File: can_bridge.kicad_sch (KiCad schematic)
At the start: 1 part, among them J9 Conn_01x05_Pin

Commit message: use Common libraries, replace TI MCU with STM32 for CAN bridge
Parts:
- J9: footprint (none) -> Connector_PinHeader_2.54mm:PinHeader_1x05_P2.54mm_Vertical
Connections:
- no-connect marks 2 -> 0
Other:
- removed sheet USB Connector
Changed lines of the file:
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@@
 		(color 0 0 0 0)
 	)
-	(junction
-		(at 84.455 69.215)
-		(diameter 0)
-		(color 0 0 0 0)
-	)
-	(junction
-		(at 84.455 62.865)
-		(diameter 0)
-		(color 0 0 0 0)
-	)
-	(no_connect
-		(at 212.09 82.55)
-	)
-	(no_connect
-		(at 212.09 85.725)
-	)
 	(wire
 		(pts
@@
 	(wire
 		(pts
-			(xy 84.455 62.865) (xy 84.455 69.215)
-		)
-		(stroke
-			(width 0)
-			(type default)
-		)
-	)
-	(wire
-		(pts
 			(xy 84.455 62.865) (xy 116.205 62.865)
 		)
@@
 	(wire
 		(pts
-			(xy 176.53 85.725) (xy 180.975 85.725)
-		)
-		(stroke
-			(width 0)
-			(type default)
-		)
-	)
-	(wire
-		(pts
 			(xy 111.76 41.91) (xy 116.205 41.91)
 		)
@@
 		(pts
 			(xy 25.4 57.785) (xy 36.195 57.785)
-		)
-		(stroke
-			(width 0)
-			(type default)
-		)
-	)
-	(wire
-		(pts
-			(xy 176.53 82.55) (xy 180.975 82.55)
 		)
 		(stroke
@@
 			)
 			(justify right)
-		)
-	)
-	(hierarchical_label "GND"
-		(shape input)
-		(at 212.09 88.9 0)
-		(fields_autoplaced yes)
-		(effects
-			(font
-				(size 1.524 1.524)
-			)
-			(justify left)
-		)
-	)
-	(hierarchical_label "GND"
-		(shape input)
-		(at 212.09 92.075 0)
-		(fields_autoplaced yes)
-		(effects
-			(font
-				(size 1.524 1.524)
-			)
-			(justify left)
 		)
 	)
@@
 			)
 		)
-		(property "Footprint" ""
+		(property "Footprint" "Connector_PinHeader_2.54mm:PinHeader_1x05_P2.54mm_Vertical"
 			(at 200.66 62.865 0)
 			(effects
@@
 	)
 	(sheet
-		(at 180.975 78.105)
-		(size 31.115 16.51)
-		(fields_autoplaced yes)
-		(stroke
-			(width 0.1524)
-			(type solid)
-		)
-		(fill
-			(color 0 0 0 0.0000)
-		)
-		(property "Sheetname" "USB Connector"
-			(at 180.975 77.3934 0)
-			(effects
-				(font
-					(size 1.27 1.27)
-				)
-				(justify left bottom)
-			)
-		)
-		(property "Sheetfile" "../avionics_board/USB.kicad_sch"
-			(at 180.975 95.1996 0)
-			(effects
-				(font
-					(size 1.27 1.27)
-				)
-				(justify left top)
-			)
-		)
-		(pin "GND1" output
-			(at 212.09 92.075 0)
-			(effects
-				(font
-					(size 1.524 1.524)
-				)
-				(justify right)
-			)
-		)
-		(pin "USB_OTG_FS_DM" bidirectional
-			(at 180.975 85.725 180)
-			(effects
-				(font
-					(size 1.524 1.524)
-				)
-				(justify left)
-			)
-		)
-		(pin "VUSB1" output
-			(at 212.09 82.55 0)
-			(effects
-				(font
-					(size 1.524 1.524)
-				)
-				(justify right)
-			)
-		)
-		(pin "GND2" output
-			(at 212.09 88.9 0)
-			(effects
-				(font
-					(size 1.524 1.524)
-				)
-				(justify right)
-			)
-		)
-		(pin "VUSB2" output
-			(at 212.09 85.725 0)
-			(effects
-				(font
-					(size 1.524 1.524)
-				)
-				(justify right)
-			)
-		)
-		(pin "USB_OTG_FS_DP" bidirectional
-			(at 180.975 82.55 180)
-			(effects
-				(font
-					(size 1.524 1.524)
-				)
-				(justify left)
-			)
-		)
-		(instances
-			(project "openlst-hw"
-				(path "/a863a5ec-a5d4-4f54-be53-e8c01d5e3ac4/53f12969-e593-459a-9671-cc23a5a9aea0"
-					(page "10")
-				)
-			)
-		)
-	)
-	(sheet
 		(at 36.83 121.285)
 		(size 28.575 13.335)
@@
 			)
 		)
-		(pin "CAN2_RX" input
+		(pin "CAN1_RX" input
 			(at 116.205 59.69 180)
 			(effects
@@
 			)
 		)
-		(pin "CAN1_RX" input
+		(pin "CAN2_RX" input
 			(at 116.205 92.075 180)
 			(effects

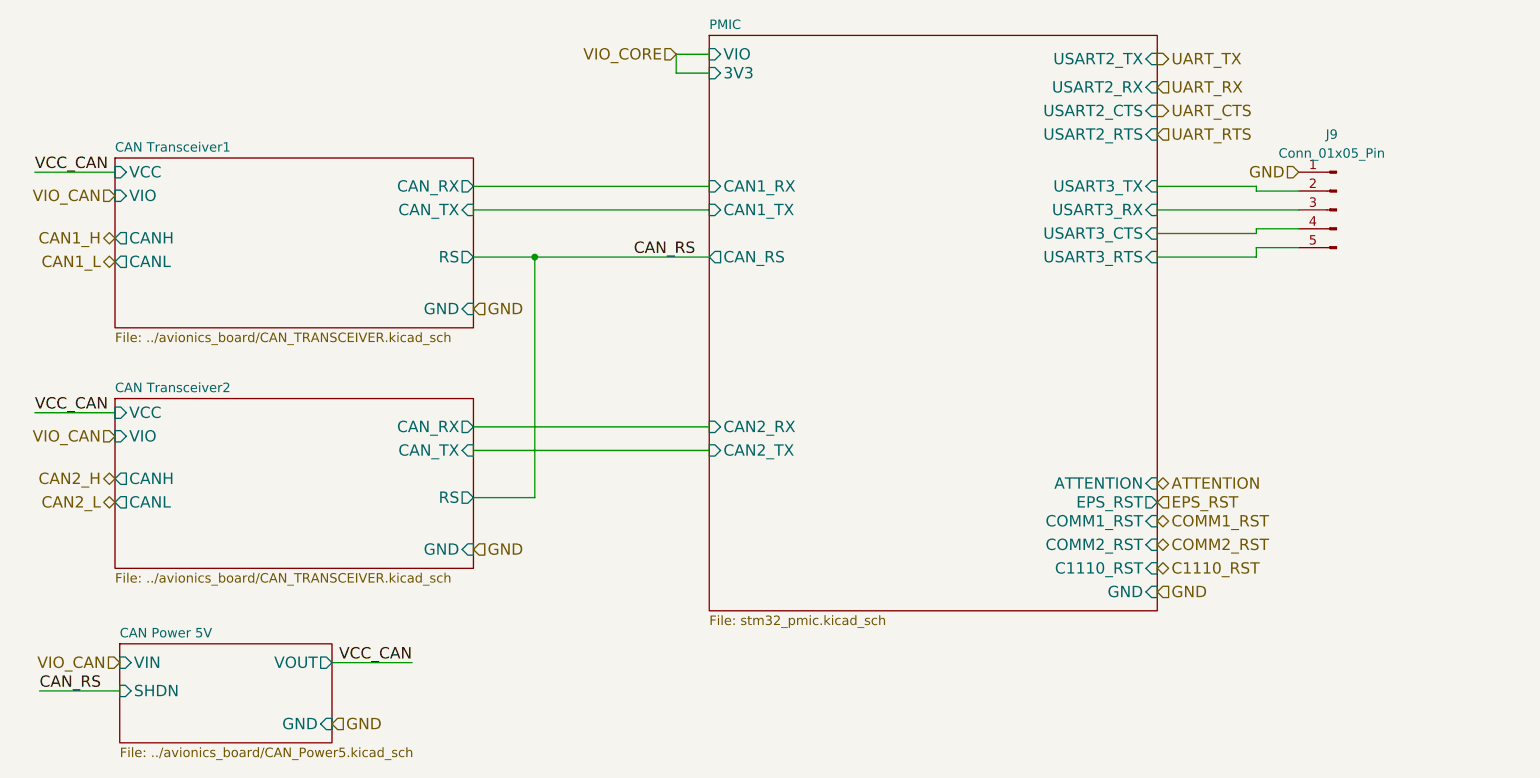
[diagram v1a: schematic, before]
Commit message: replacd TJA1042 with TCAN3414 that allows differential from 3V, negating the need for 5V generator
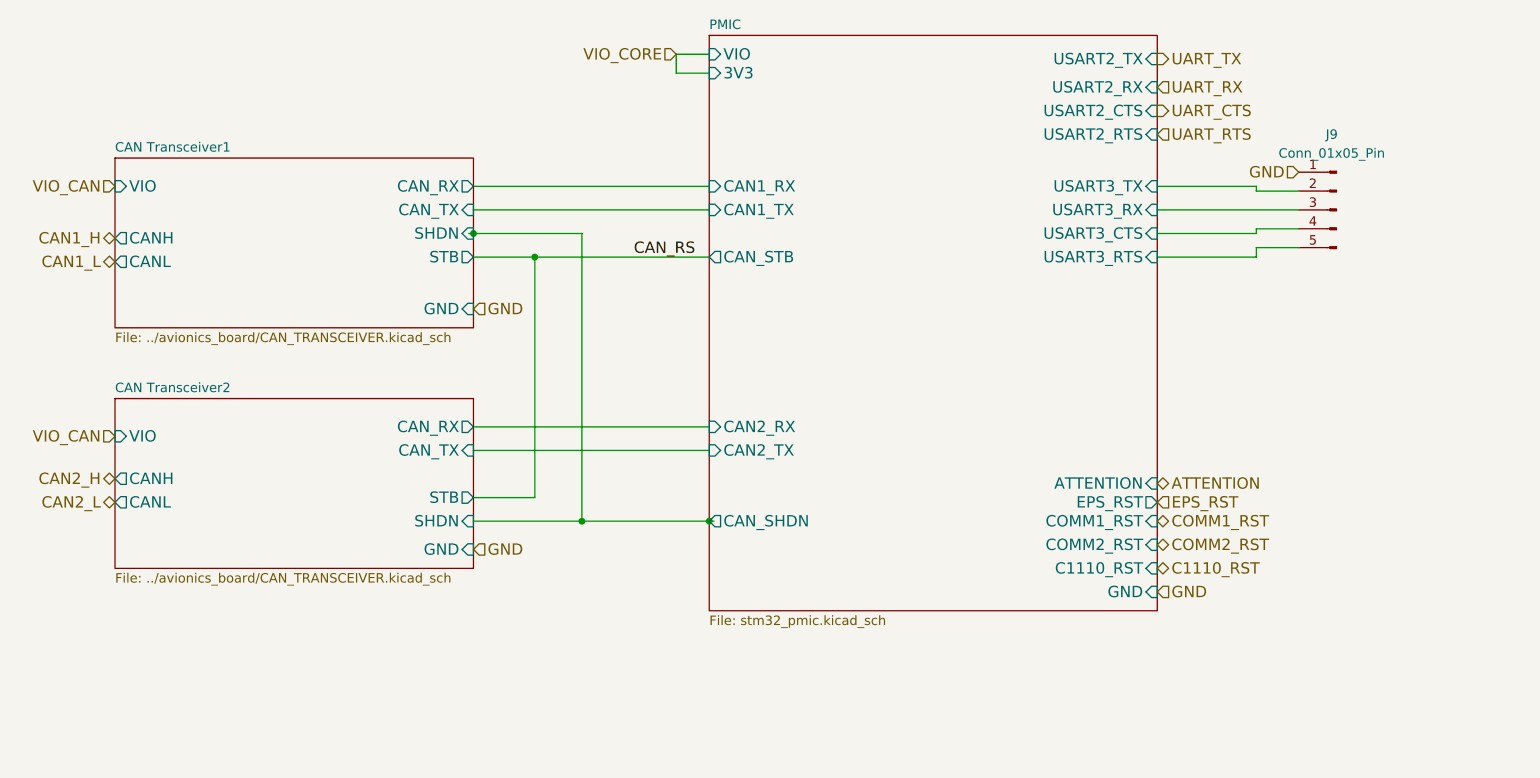
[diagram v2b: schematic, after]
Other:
- removed sheet CAN Power 5V
- sheet CAN Transceiver1 ports: added SHDN, STB; removed RS, VCC
- sheet CAN Transceiver2 ports: added SHDN, STB; removed RS, VCC
- sheet PMIC ports: added CAN_SHDN, CAN_STB; removed CAN_RS
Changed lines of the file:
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@@
 	(paper "A4")
+	(junction
+		(at 116.205 104.775)
+		(diameter 0)
+		(color 0 0 0 0)
+	)
 	(junction
 		(at 92.71 69.215)
@@
 		(color 0 0 0 0)
 	)
+	(junction
+		(at 99.06 104.775)
+		(diameter 0)
+		(color 0 0 0 0)
+	)
+	(junction
+		(at 84.455 66.04)
+		(diameter 0)
+		(color 0 0 0 0)
+	)
 	(wire
 		(pts
@@
 	(wire
 		(pts
+			(xy 84.455 104.775) (xy 99.06 104.775)
+		)
+		(stroke
+			(width 0)
+			(type default)
+		)
+	)
+	(wire
+		(pts
 			(xy 84.455 62.865) (xy 116.205 62.865)
 		)
@@
 	(wire
 		(pts
-			(xy 26.035 127.635) (xy 36.83 127.635)
-		)
-		(stroke
-			(width 0)
-			(type default)
-		)
-	)
-	(wire
-		(pts
-			(xy 76.2 123.825) (xy 65.405 123.825)
+			(xy 116.205 104.775) (xy 116.84 104.775)
 		)
 		(stroke
@@
 	(wire
 		(pts
+			(xy 99.06 66.04) (xy 99.06 104.775)
+		)
+		(stroke
+			(width 0)
+			(type default)
+		)
+	)
+	(wire
+		(pts
 			(xy 111.76 44.45) (xy 116.205 44.45)
 		)
@@
 	(wire
 		(pts
+			(xy 99.06 104.775) (xy 116.205 104.775)
+		)
+		(stroke
+			(width 0)
+			(type default)
+		)
+	)
+	(wire
+		(pts
 			(xy 176.53 69.215) (xy 189.865 69.215)
 		)
@@
 	(wire
 		(pts
-			(xy 25.4 57.785) (xy 36.195 57.785)
+			(xy 83.82 66.04) (xy 84.455 66.04)
+		)
+		(stroke
+			(width 0)
+			(type default)
+		)
+	)
+	(wire
+		(pts
+			(xy 84.455 66.04) (xy 99.06 66.04)
 		)
 		(stroke
@@
 	(wire
 		(pts
-			(xy 25.4 90.17) (xy 36.195 90.17)
-		)
-		(stroke
-			(width 0)
-			(type default)
-		)
-	)
-	(wire
-		(pts
 			(xy 189.865 66.04) (xy 189.865 65.405)
 		)
@@
 			(width 0)
 			(type default)
-		)
-	)
-	(label "VCC_CAN"
-		(at 25.4 57.785 0)
-		(fields_autoplaced yes)
-		(effects
-			(font
-				(size 1.524 1.524)
-			)
-			(justify left bottom)
-		)
-	)
-	(label "VCC_CAN"
-		(at 25.4 90.17 0)
-		(fields_autoplaced yes)
-		(effects
-			(font
-				(size 1.524 1.524)
-			)
-			(justify left bottom)
-		)
-	)
-	(label "CAN_RS"
-		(at 26.035 127.635 0)
-		(fields_autoplaced yes)
-		(effects
-			(font
-				(size 1.524 1.524)
-			)
-			(justify left bottom)
-		)
-	)
-	(label "VCC_CAN"
-		(at 76.2 123.825 180)
-		(fields_autoplaced yes)
-		(effects
-			(font
-				(size 1.524 1.524)
-			)
-			(justify right bottom)
 		)
 	)
@@
 	(hierarchical_label "VIO_CAN"
 		(shape input)
-		(at 36.195 60.96 180)
+		(at 36.195 59.69 180)
 		(fields_autoplaced yes)
 		(effects
@@
 		)
 	)
-	(hierarchical_label "VIO_CAN"
-		(shape input)
-		(at 36.83 123.825 180)
-		(fields_autoplaced yes)
-		(effects
-			(font
-				(size 1.524 1.524)
-			)
-			(justify right)
-		)
-	)
 	(hierarchical_label "UART_RX"
 		(shape input)
@@
 		(shape output)
 		(at 176.53 49.53 0)
-		(fields_autoplaced yes)
-		(effects
-			(font
-				(size 1.524 1.524)
-			)
-			(justify left)
-		)
-	)
-	(hierarchical_label "GND"
-		(shape input)
-		(at 65.405 132.08 0)
 		(fields_autoplaced yes)
 		(effects
@@
 		)
 		(pin "VIO" input
-			(at 36.195 60.96 180)
+			(at 36.195 59.69 180)
 			(effects
 				(font
@@
 			)
 		)
-		(pin "RS" output
-			(at 84.455 69.215 0)
-			(effects
-				(font
-					(size 1.524 1.524)
-				)
-				(justify right)
-			)
-		)
-		(pin "VCC" input
-			(at 36.195 57.785 180)
-			(effects
-				(font
-					(size 1.524 1.524)
-				)
-				(justify left)
-			)
-		)
 		(pin "CANL" output
 			(at 36.195 69.85 180)
@@
 				)
 				(justify left)
+			)
+		)
+		(pin "SHDN" input
+			(at 84.455 66.04 0)
+			(effects
+				(font
+					(size 1.524 1.524)
+				)
+				(justify right)
+			)
+		)
+		(pin "STB" output
+			(at 84.455 69.215 0)
+			(effects
+				(font
+					(size 1.524 1.524)
+				)
+				(justify right)
 			)
 		)
@@
 	)
 	(sheet
-		(at 36.83 121.285)
-		(size 28.575 13.335)
+		(at 36.195 88.265)
+		(size 48.26 22.86)
 		(fields_autoplaced yes)
 		(stroke
@@
 			(color 0 0 0 0.0000)
 		)
-		(property "Sheetname" "CAN Power 5V"
-			(at 36.83 120.5734 0)
-			(effects
-				(font
-					(size 1.27 1.27)
-				)
-				(justify left bottom)
-			)
-		)
-		(property "Sheetfile" "../avionics_board/CAN_Power5.kicad_sch"
-			(at 36.83 135.2046 0)
-			(effects
-				(font
-					(size 1.27 1.27)
-				)
-				(justify left top)
-			)
-		)
-		(pin "GND" input
-			(at 65.405 132.08 0)
-			(effects
-				(font
-					(size 1.524 1.524)
-				)
-				(justify right)
-			)
-		)
-		(pin "VIN" input
-			(at 36.83 123.825 180)
-			(effects
-				(font
-					(size 1.524 1.524)
-				)
-				(justify left)
-			)
-		)
-		(pin "SHDN" input
-			(at 36.83 127.635 180)
-			(effects
-				(font
-					(size 1.524 1.524)
-				)
-				(justify left)
-			)
-		)
-		(pin "VOUT" output
-			(at 65.405 123.825 0)
-			(effects
-				(font
-					(size 1.524 1.524)
-				)
-				(justify right)
-			)
-		)
-		(instances
-			(project "openlst-hw"
-				(path "/a863a5ec-a5d4-4f54-be53-e8c01d5e3ac4/53f12969-e593-459a-9671-cc23a5a9aea0"
-					(page "9")
-				)
-			)
-		)
-	)
-	(sheet
-		(at 36.195 88.265)
-		(size 48.26 22.86)
-		(fields_autoplaced yes)
-		(stroke
-			(width 0.1524)
-			(type solid)
-		)
-		(fill
-			(color 0 0 0 0.0000)
-		)
 		(property "Sheetname" "CAN Transceiver2"
 			(at 36.195 87.5534 0)
@@
 			)
 		)
-		(pin "RS" output
-			(at 84.455 101.6 0)
-			(effects
-				(font
-					(size 1.524 1.524)
-				)
-				(justify right)
-			)
-		)
-		(pin "VCC" input
-			(at 36.195 90.17 180)
-			(effects
-				(font
-					(size 1.524 1.524)
-				)
-				(justify left)
-			)
-		)
 		(pin "CANL" output
 			(at 36.195 102.235 180)
@@
 				)
 				(justify left)
+			)
+		)
+		(pin "SHDN" input
+			(at 84.455 104.775 0)
+			(effects
+				(font
+					(size 1.524 1.524)
+				)
+				(justify right)
+			)
+		)
+		(pin "STB" output
+			(at 84.455 101.6 0)
+			(effects
+				(font
+					(size 1.524 1.524)
+				)
+				(justify right)
 			)
 		)
@@
 			)
 		)
-		(pin "CAN_RS" output
+		(pin "CAN_STB" output
 			(at 116.205 69.215 180)
 			(effects
@@
 			)
 		)
+		(pin "CAN_SHDN" output
+			(at 116.205 104.775 180)
+			(effects
+				(font
+					(size 1.524 1.524)
+				)
+				(justify left)
+			)
+		)
